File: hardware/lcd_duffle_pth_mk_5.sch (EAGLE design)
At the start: 14 parts, among them IC1 ATTINY84, IC2 WS2811

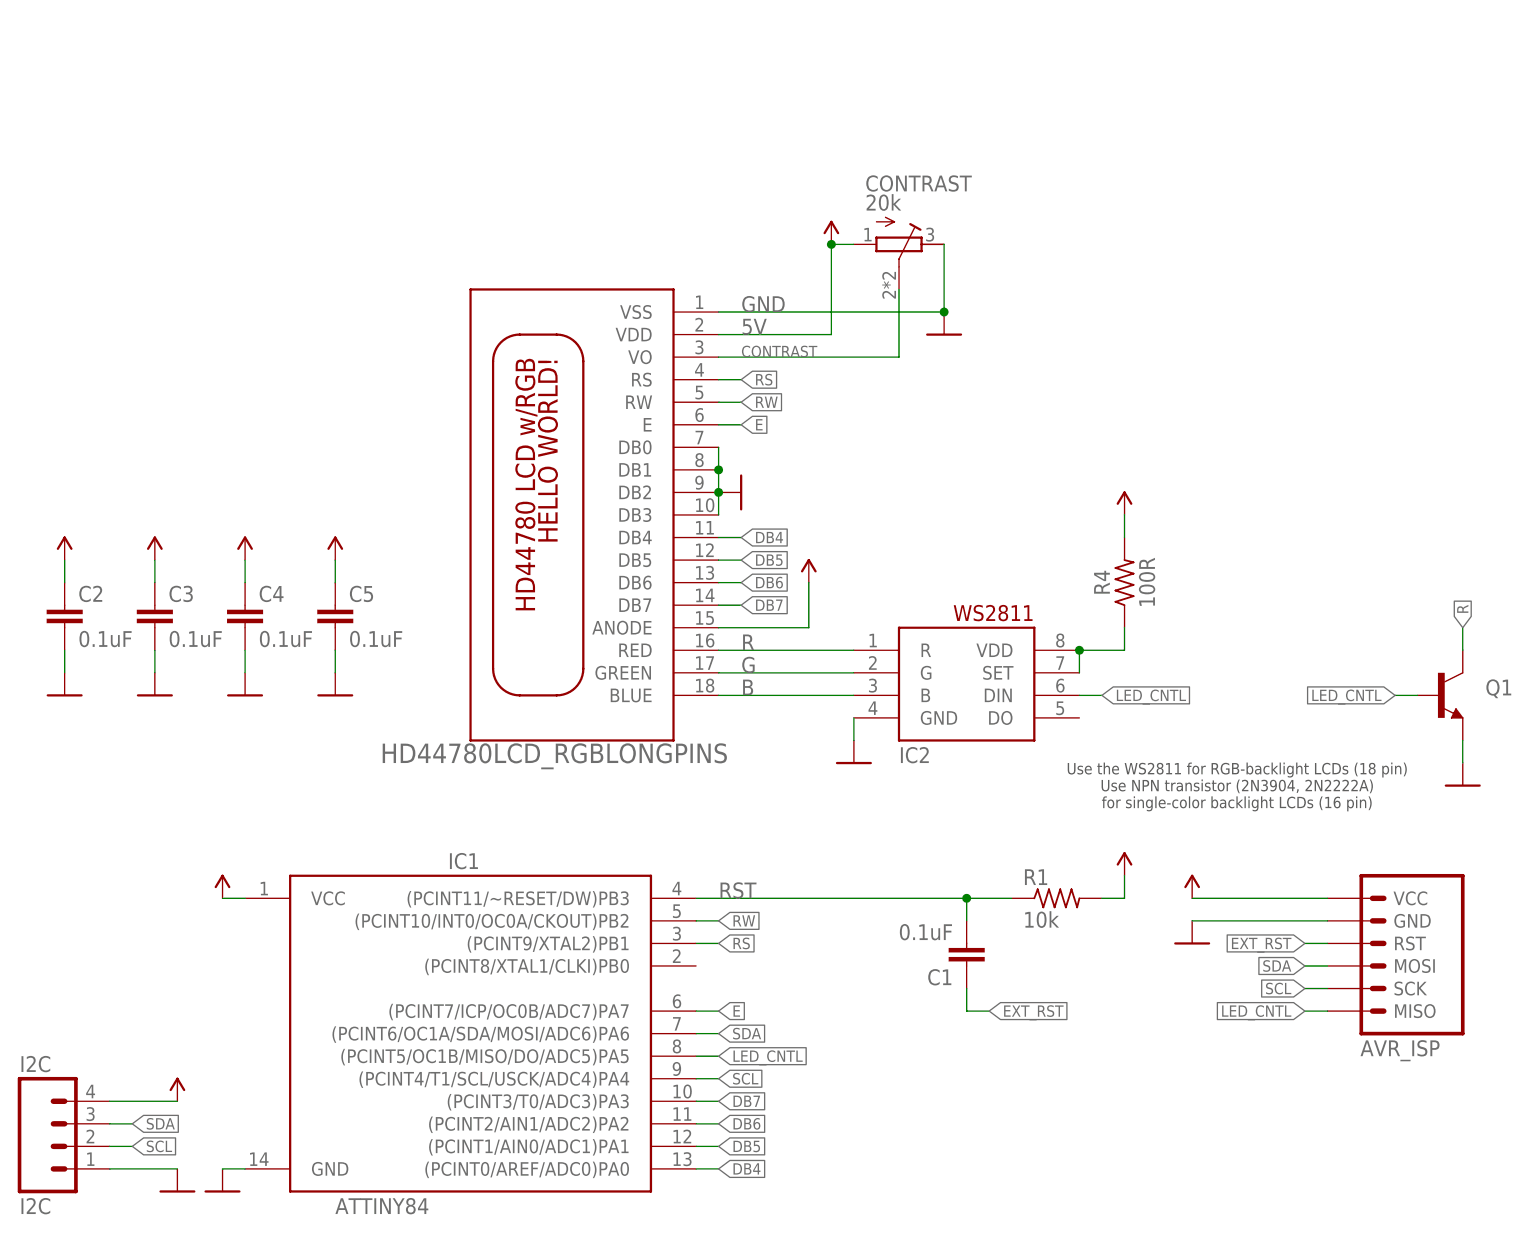
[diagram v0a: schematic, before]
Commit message: revised board to add i2c pullups, relayout to reduce vias since most were due to poor planning, and remove cap from external reset line as it shouldn't be needed according to atmel's docs
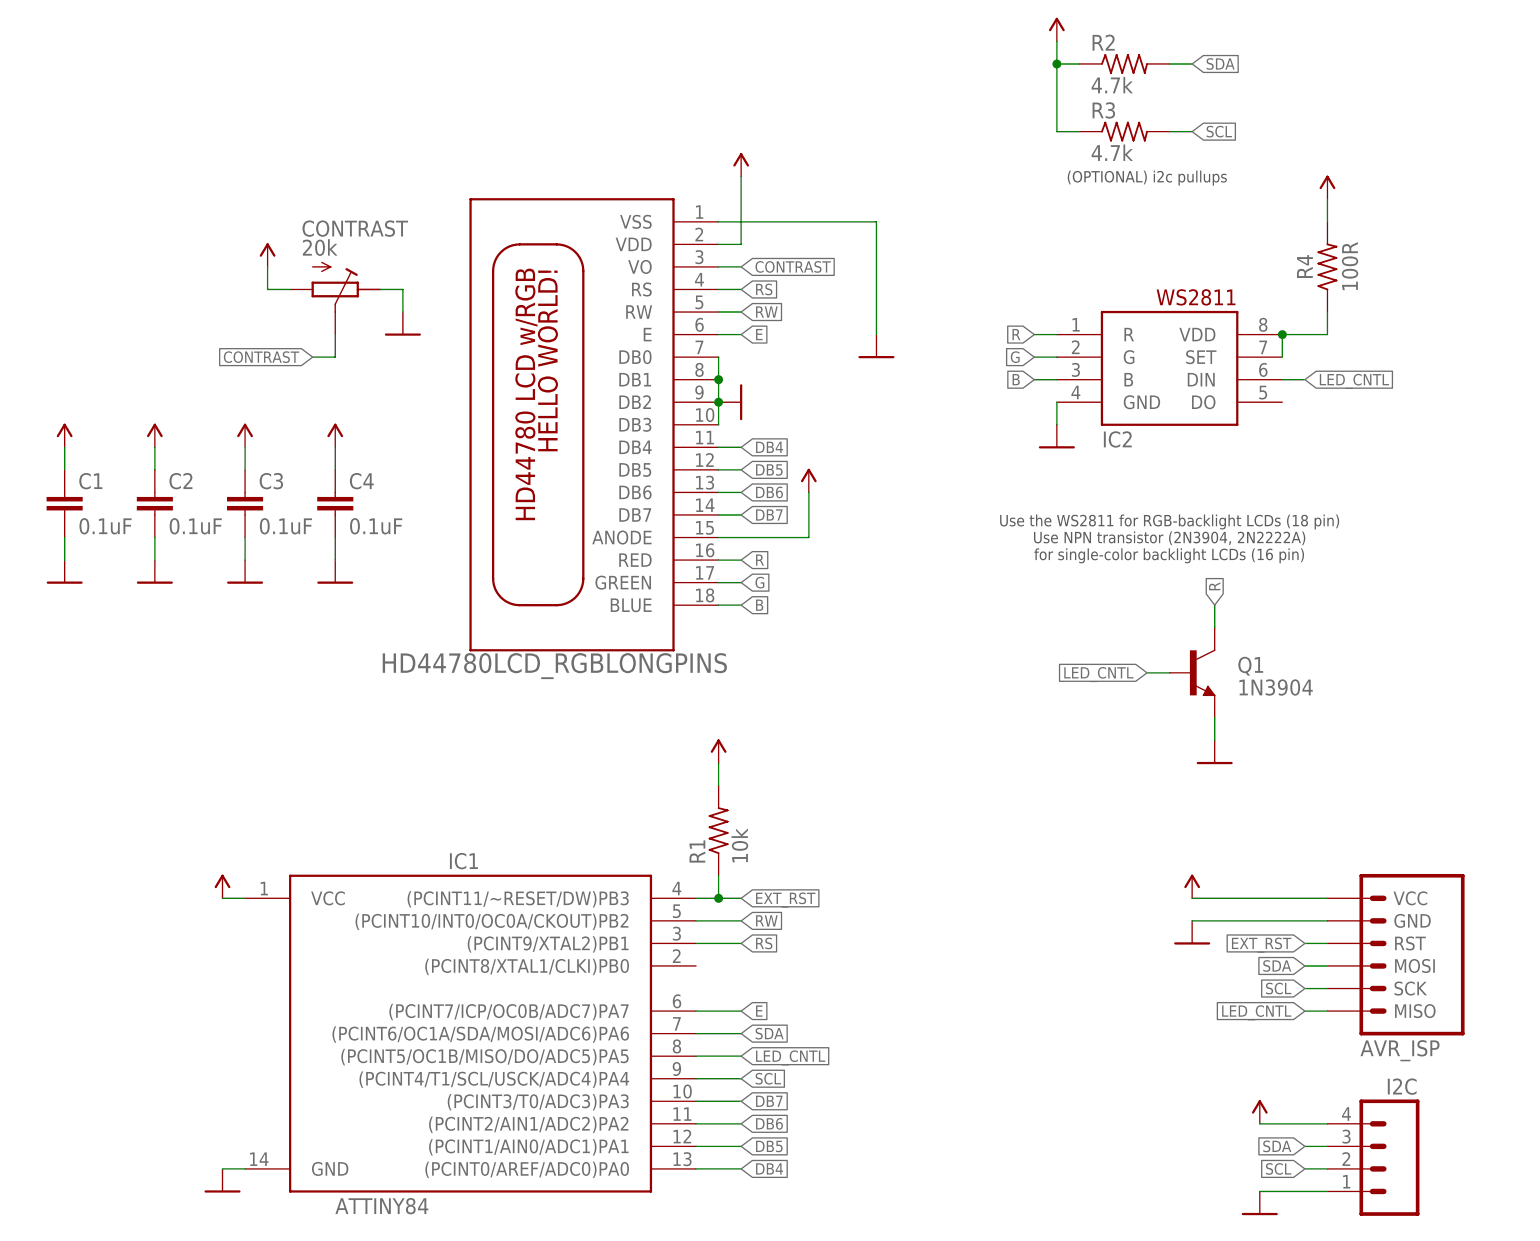
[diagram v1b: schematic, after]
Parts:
- removed C5: 0.1uF, A_butts:CAPACITOR-CERAMIC025-024X044
- added R2, R3: 4.7k, A_butts:RESISTORPTH-AXIAL-5.08MM
- I2C: value I2C -> M04JST_XH_RA
- Q1: value (none) -> 1N3904
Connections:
- removed net RST: C1.2, IC1.(PCINT11/~RESET/DW)PB3, R1.1
- net 5V: now also C1.2, R2.1, R3.1; no longer C5.2
- net EXT_RST: now also IC1.(PCINT11/~RESET/DW)PB3, R1.1; no longer C1.1
- net GND: now also C1.1; no longer C5.1
- net SCL: now also R3.2
- net SDA: now also R2.2
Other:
- note added: "(OPTIONAL) i2c pullups"
- moved on the sheet: C1, C2, C3, C4, I2C, IC2, Q1, R1, R4
